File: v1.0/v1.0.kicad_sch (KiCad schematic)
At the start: 6 parts, among them J1 Conn_01x05_Pin, J2 Conn_01x02_Pin, J3 Conn_01x02_Pin, J4 Conn_01x02_Pin, J5 Conn_01x02_Pin, J6 Conn_01x02_Pin

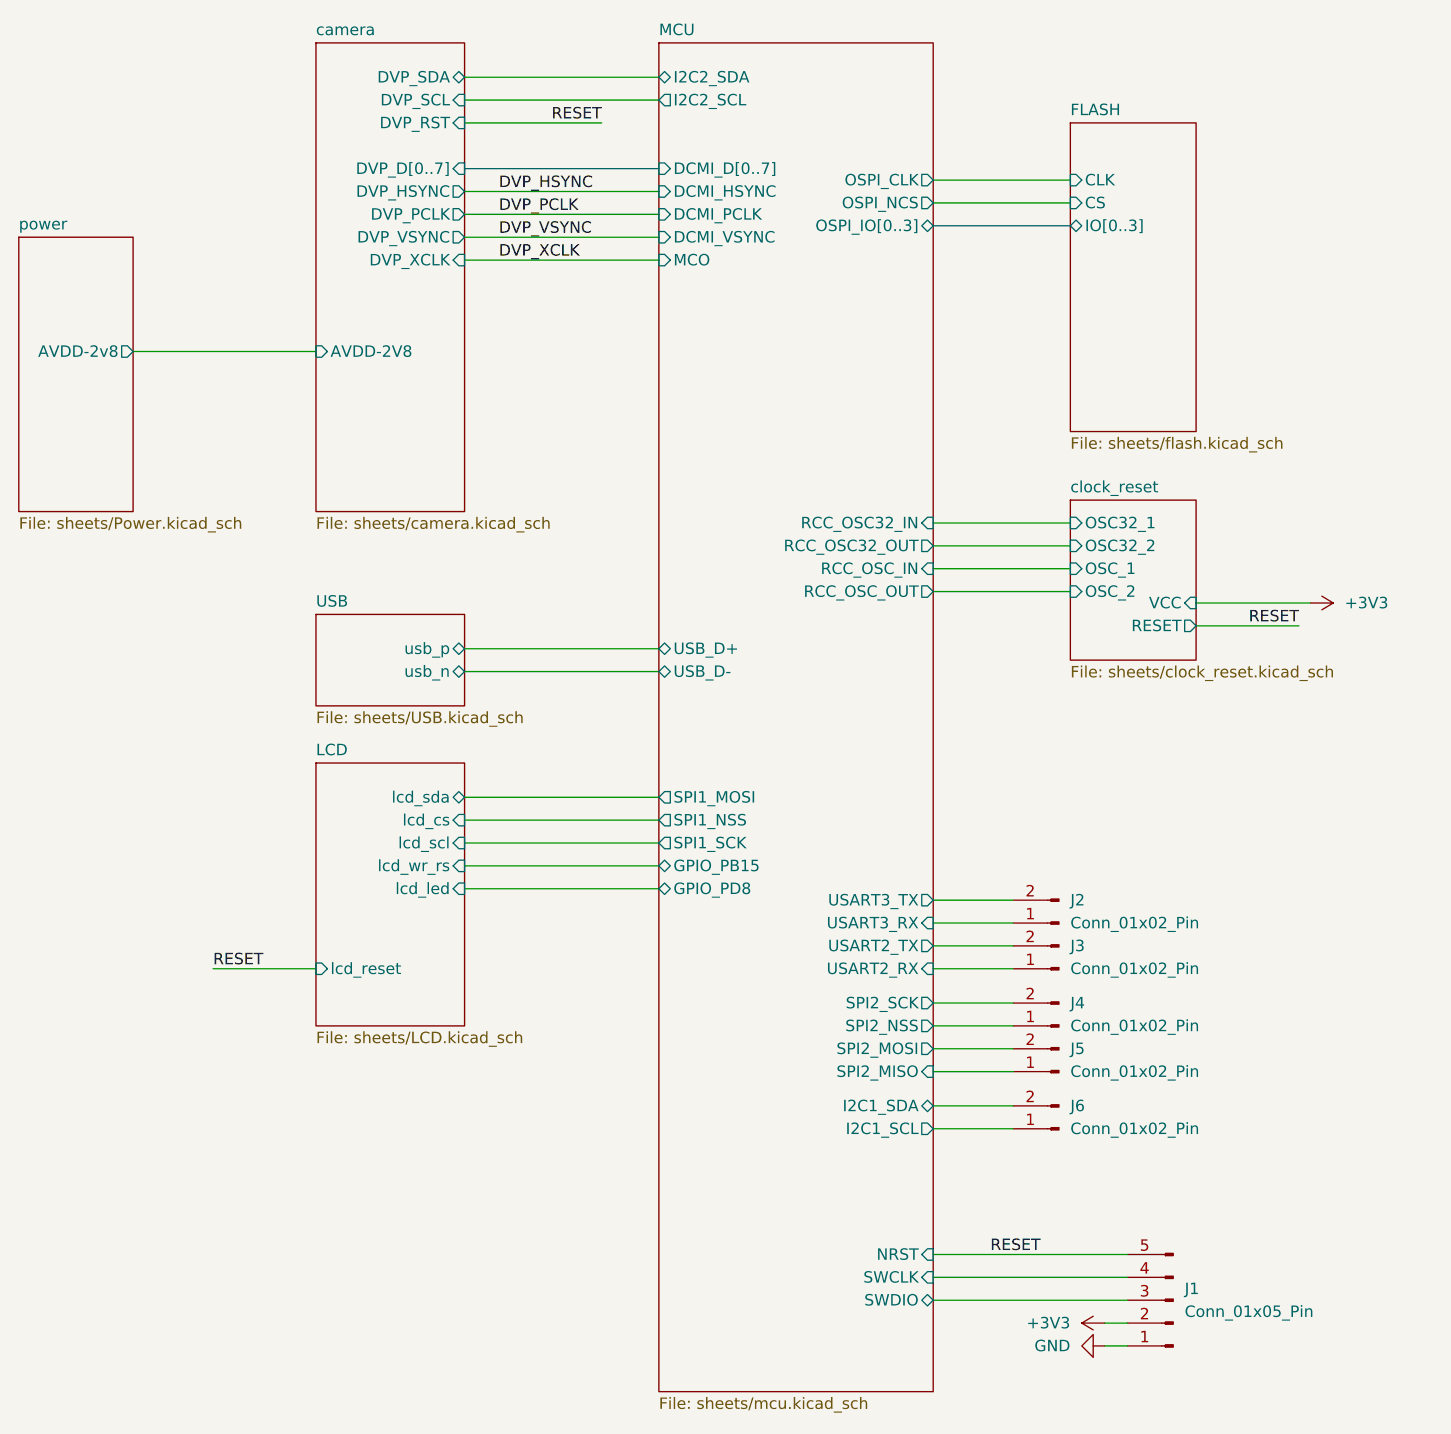
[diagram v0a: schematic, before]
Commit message: V1.0 rework to match stm32u5xxxQ
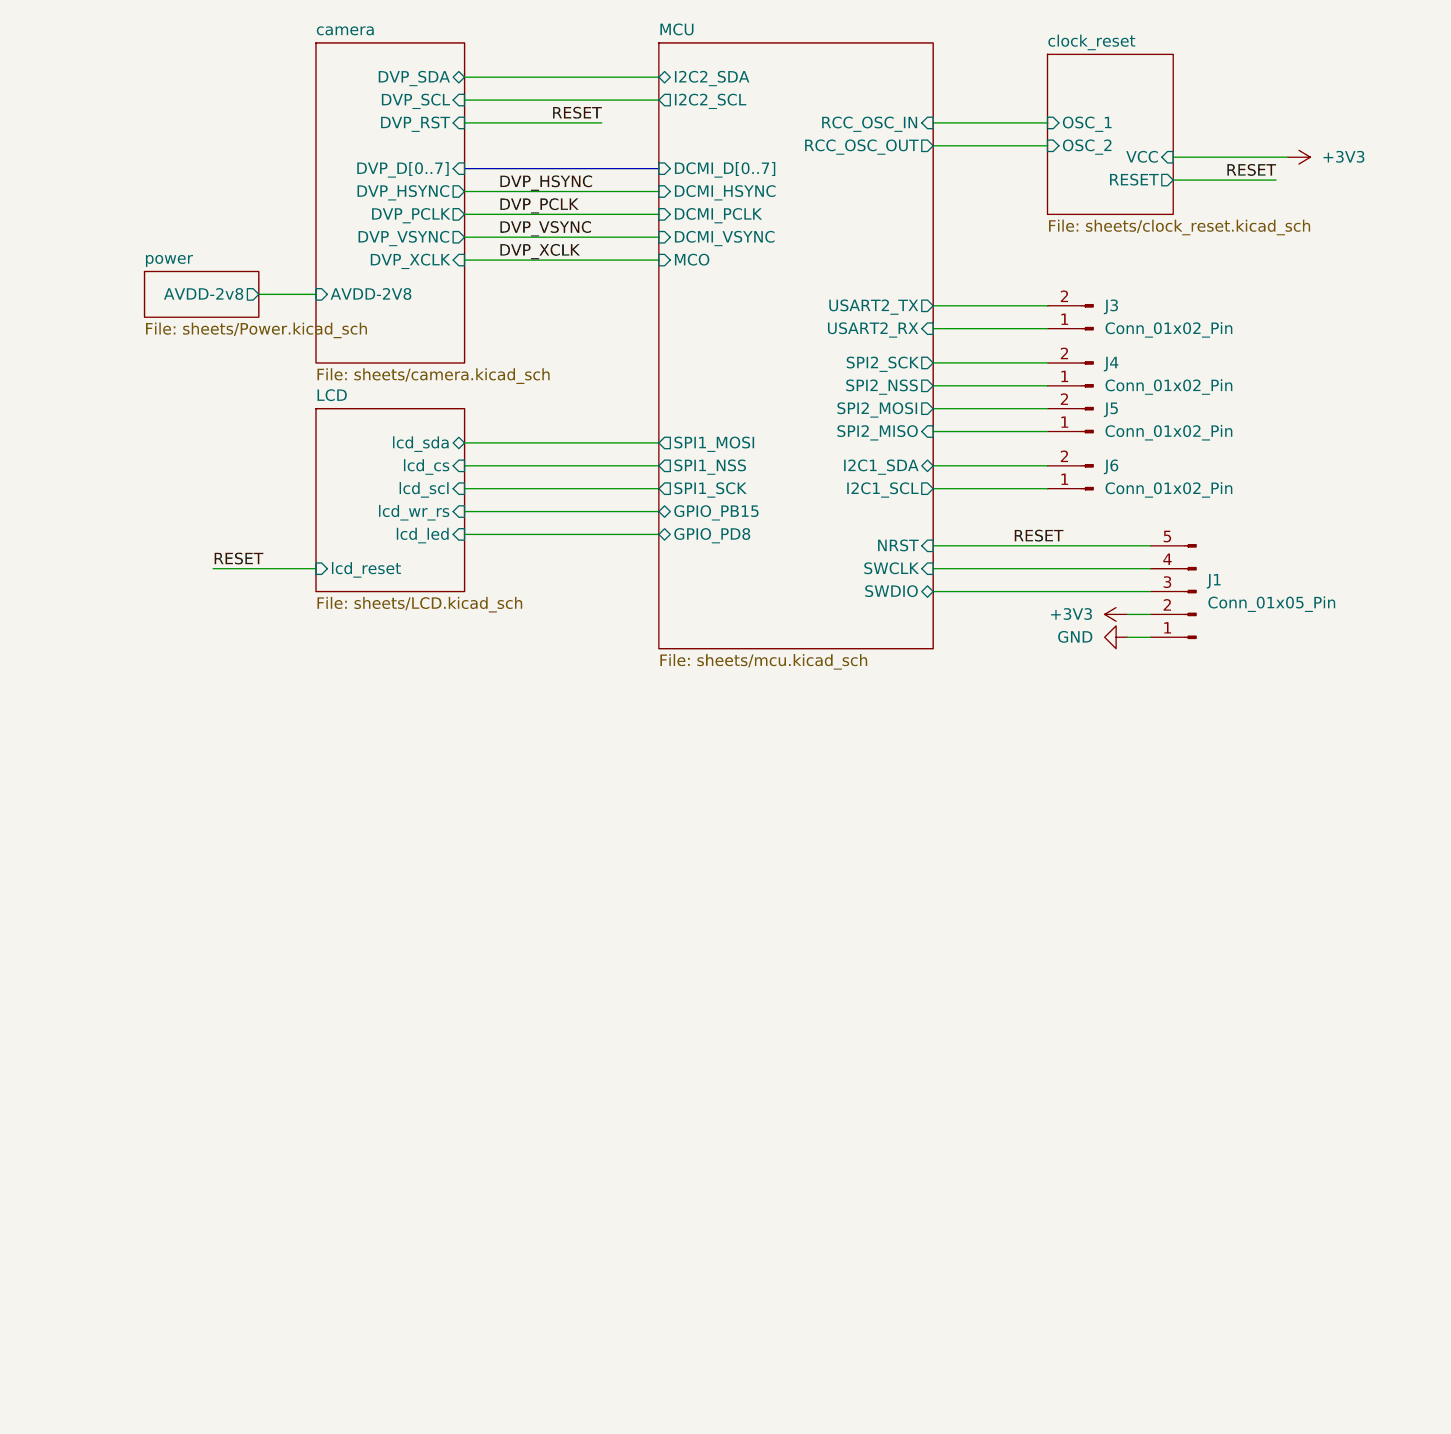
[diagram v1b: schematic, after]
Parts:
- removed J2: Conn_01x02_Pin, Connector_PinHeader_2.54mm:PinHeader_1x02_P2.54mm_Vertical, symbol Connector:Conn_01x02_Pin
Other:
- removed sheet FLASH
- removed sheet USB
- sheet MCU ports: added none; removed OSPI_CLK, OSPI_IO[0..3], OSPI_NCS, RCC_OSC32_IN, RCC_OSC32_OUT, USART3_RX, USART3_TX, USB_D+, USB_D-
- sheet clock_reset ports: added none; removed OSC32_1, OSC32_2
- moved on the sheet: J1, J3, J4, J5, J6
